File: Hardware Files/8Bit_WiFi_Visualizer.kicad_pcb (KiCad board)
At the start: 2 copper layers, 60 x 45 mm, 29 parts, among them J1 USB_B_Micro, J2 Conn_01x04, J3 Conn_01x01, J4 Conn_01x01, SW1 SW_Push_Dual, SW2 SW_SPST, SW3 SW_SPST, U1 3.3V 1A, U2 74HC595, U3 ESP-WROOM-02D

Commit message: Re-Annotate PCB
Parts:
- removed G***: LOGO, 8Bit_WiFi_Visualizer_Footprints:logo
- renumbered C3 to C1, C4 to C3, C5 to C4, C6 to C5, R12 to R1, R11 to R2, R10 to R3, R13 to R4, R1 to R5

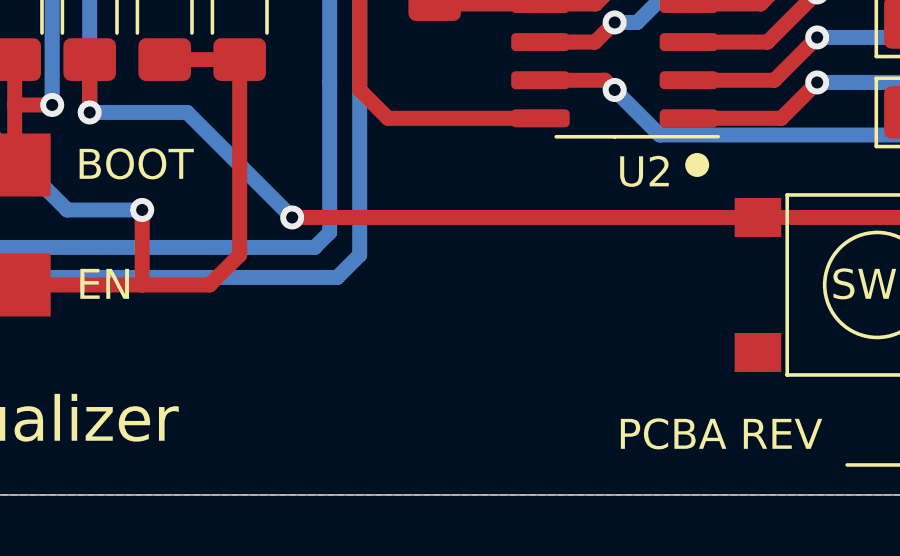
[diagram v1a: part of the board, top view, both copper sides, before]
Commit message: Add missing logo
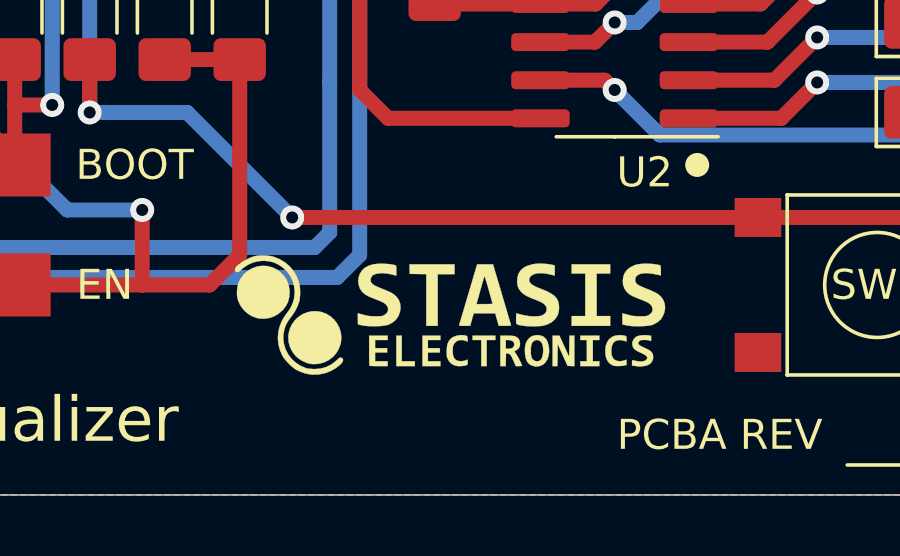
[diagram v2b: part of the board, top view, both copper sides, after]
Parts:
- added G***: LOGO, 8Bit_WiFi_Visualizer_Footprints:logo, F.Cu at (35.5, 39.0)
